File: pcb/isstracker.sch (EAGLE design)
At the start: 22 parts, among them IC1 SN74AHCT125N, IC2 L7805CV, J1 MOTOR_RIGHT, J2 MOTOR_LEFT, J4 DISPLAY, J5 CONTROL, J7 LED, J8 UART, J9 DISTANCE, U1 ARGON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

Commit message: Lots of changes
* Dropped LED's and LASER control
* Renamed DECLINATION to AZIMUTH
* Moved AZIMUTH control hookup into the globe (it needs to spin freely)

I couldn't make the LED's fit and shine without casting shadows inside
the globe. Plus, there wasn't much room, and it required more wires to
make work. No a critical problem, but the challenges outweighed the
benefits. I'm going to water color paint the globe now.

I also removed the LASER control, the manufacturer said don't duty cycle
it, the built in controls take care of it. This isn't supposed to be on
constantly anyway.
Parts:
- removed IC1: SN74AHCT125N, adafruit:74125N
- removed J2: MOTOR_LEFT, SparkFun-Connectors:CONN_11
- removed J7: LED, SparkFun-Connectors:CONN_04
- added J3: MOTOR_LEFT, SparkFun-Connectors:CONN_12
- J5: device SparkFun-Connectors:CONN_09 -> SparkFun-Connectors:CONN_08"
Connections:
- removed net CO: IC1A.O, J7.2
- removed net DO: IC1B.O, J7.3
- removed net LASER: J5.9, U1.A0
- removed net LED_CO: IC1A.I, U1.D7
- removed net LED_DO: IC1B.I, U1.D8
- net +5V: no longer IC1P.VCC, J7.4
- net AZIMUTH: now also U1.D7; no longer U1.A1
- net GND: now also J3.3; no longer IC1A.OE, IC1B.OE, IC1C.O, IC1C.OE, IC1D.O, IC1D.OE, IC1P.GND, J2.3, J7.1
- net MTR_DIR: now also J3.1; no longer J2.1
- net MTR_MS1: now also J3.10; no longer J2.10
- net MTR_SLP: now also J3.11; no longer J2.11
- net MTR_STEP: now also J3.2; no longer J2.2

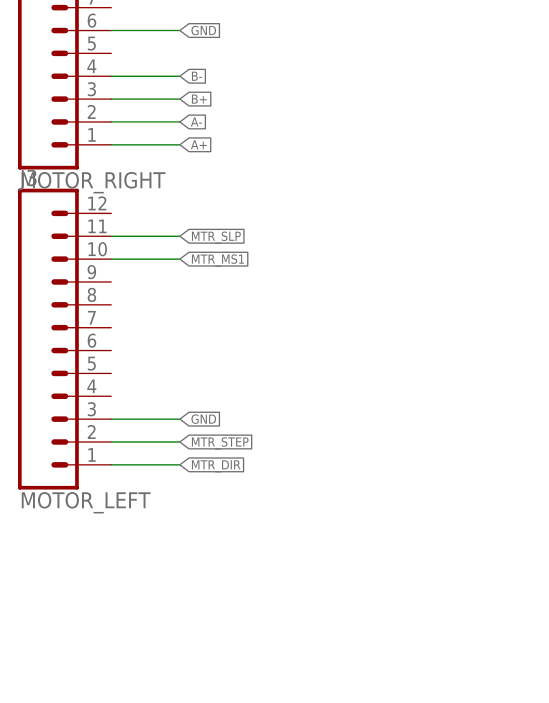
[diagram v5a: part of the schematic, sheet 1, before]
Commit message: PCB fixups
* Bumped PCB revisions
* Layout changes and some silk screen updates
* No functionality changes
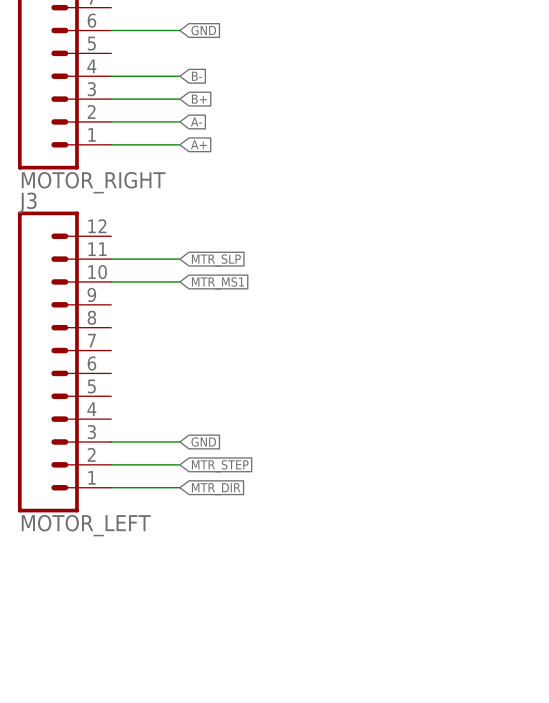
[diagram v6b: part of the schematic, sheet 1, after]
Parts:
- H1, H2, H3, H4: value STAND-OFF -> MOUNT-HOLE3.0; device SparkFun-Hardware:STAND-OFF -> holes:MOUNT-HOLE3.0
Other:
- moved on the sheet: J3
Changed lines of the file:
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@@
 <part name="LED1" library="adafruit" library_urn="urn:adsk.eagle:library:420" deviceset="LED" device="3MM" package3d_urn="urn:adsk.eagle:package:6240537/1" value="RED"/>
 <part name="R1" library="SparkFun-Resistors" library_urn="urn:adsk.eagle:library:532" deviceset="0.3OHM" device="-0805-1/8W-1%" package3d_urn="urn:adsk.eagle:package:39651/1" value="1k"/>
-<part name="H2" library="SparkFun-Hardware" library_urn="urn:adsk.eagle:library:519" deviceset="STAND-OFF" device="" package3d_urn="urn:adsk.eagle:package:38630/1"/>
-<part name="H3" library="SparkFun-Hardware" library_urn="urn:adsk.eagle:library:519" deviceset="STAND-OFF" device="" package3d_urn="urn:adsk.eagle:package:38630/1"/>
-<part name="H4" library="SparkFun-Hardware" library_urn="urn:adsk.eagle:library:519" deviceset="STAND-OFF" device="" package3d_urn="urn:adsk.eagle:package:38630/1"/>
 <part name="C2" library="SparkFun-Capacitors" library_urn="urn:adsk.eagle:library:510" deviceset="100UF-POLAR" device="-RADIAL-2.5MM-25V-20%" package3d_urn="urn:adsk.eagle:package:37415/1" value="100uF"/>
 <part name="C1" library="SparkFun-Capacitors" library_urn="urn:adsk.eagle:library:510" deviceset="100UF-POLAR" device="-RADIAL-2.5MM-25V-20%" package3d_urn="urn:adsk.eagle:package:37415/1" value="100uF"/>
-<part name="H1" library="SparkFun-Hardware" library_urn="urn:adsk.eagle:library:519" deviceset="STAND-OFF" device="" package3d_urn="urn:adsk.eagle:package:38630/1"/>
 <part name="J5" library="SparkFun-Connectors" library_urn="urn:adsk.eagle:library:513" deviceset="CONN_08" device="&quot;" package3d_urn="urn:adsk.eagle:package:38138/1" value="CONTROL"/>
 <part name="J3" library="SparkFun-Connectors" library_urn="urn:adsk.eagle:library:513" deviceset="CONN_12" device="" package3d_urn="urn:adsk.eagle:package:38169/1" value="MOTOR_LEFT"/>
+<part name="H1" library="holes" library_urn="urn:adsk.eagle:library:237" deviceset="MOUNT-HOLE" device="3.0" package3d_urn="urn:adsk.eagle:package:14277/1"/>
+<part name="H2" library="holes" library_urn="urn:adsk.eagle:library:237" deviceset="MOUNT-HOLE" device="3.0" package3d_urn="urn:adsk.eagle:package:14277/1"/>
+<part name="H3" library="holes" library_urn="urn:adsk.eagle:library:237" deviceset="MOUNT-HOLE" device="3.0" package3d_urn="urn:adsk.eagle:package:14277/1"/>
+<part name="H4" library="holes" library_urn="urn:adsk.eagle:library:237" deviceset="MOUNT-HOLE" device="3.0" package3d_urn="urn:adsk.eagle:package:14277/1"/>
 </parts>
 <sheets>
@@
 <attribute name="NAME" x="103.632" y="48.26" size="1.778" layer="95" font="vector" rot="R90"/>
 </instance>
-<instance part="J3" gate="G$1" x="10.16" y="149.86" smashed="yes">
-<attribute name="VALUE" x="10.16" y="129.794" size="1.778" layer="96" font="vector"/>
-<attribute name="NAME" x="10.16" y="165.608" size="1.778" layer="95" font="vector"/>
+<instance part="J3" gate="G$1" x="10.16" y="147.32" smashed="yes">
+<attribute name="VALUE" x="10.16" y="127.254" size="1.778" layer="96" font="vector"/>
+<attribute name="NAME" x="10.16" y="163.068" size="1.778" layer="95" font="vector"/>
 </instance>
 </instances>
@@
 </segment>
 <segment>
-<wire x1="20.32" y1="139.7" x2="27.94" y2="139.7" width="0.1524" layer="91"/>
-<label x="27.94" y="139.7" size="1.016" layer="95" xref="yes"/>
+<wire x1="20.32" y1="137.16" x2="27.94" y2="137.16" width="0.1524" layer="91"/>
+<label x="27.94" y="137.16" size="1.016" layer="95" xref="yes"/>
 <pinref part="J3" gate="G$1" pin="3"/>
 </segment>
@@
 <net name="MTR_MS1" class="0">
 <segment>
-<wire x1="20.32" y1="157.48" x2="27.94" y2="157.48" width="0.1524" layer="91"/>
-<label x="27.94" y="157.48" size="1.016" layer="95" xref="yes"/>
+<wire x1="20.32" y1="154.94" x2="27.94" y2="154.94" width="0.1524" layer="91"/>
+<label x="27.94" y="154.94" size="1.016" layer="95" xref="yes"/>
 <pinref part="J3" gate="G$1" pin="10"/>
 </segment>
@@
 <net name="MTR_STEP" class="0">
 <segment>
-<wire x1="20.32" y1="137.16" x2="27.94" y2="137.16" width="0.1524" layer="91"/>
-<label x="27.94" y="137.16" size="1.016" layer="95" xref="yes"/>
+<wire x1="20.32" y1="134.62" x2="27.94" y2="134.62" width="0.1524" layer="91"/>
+<label x="27.94" y="134.62" size="1.016" layer="95" xref="yes"/>
 <pinref part="J3" gate="G$1" pin="2"/>
 </segment>
@@
 <net name="MTR_DIR" class="0">
 <segment>
-<wire x1="20.32" y1="134.62" x2="27.94" y2="134.62" width="0.1524" layer="91"/>
-<label x="27.94" y="134.62" size="1.016" layer="95" xref="yes"/>
+<wire x1="20.32" y1="132.08" x2="27.94" y2="132.08" width="0.1524" layer="91"/>
+<label x="27.94" y="132.08" size="1.016" layer="95" xref="yes"/>
 <pinref part="J3" gate="G$1" pin="1"/>
 </segment>
@@
 <net name="MTR_SLP" class="0">
 <segment>
-<wire x1="20.32" y1="160.02" x2="27.94" y2="160.02" width="0.1524" layer="91"/>
-<label x="27.94" y="160.02" size="1.016" layer="95" xref="yes"/>
+<wire x1="20.32" y1="157.48" x2="27.94" y2="157.48" width="0.1524" layer="91"/>
+<label x="27.94" y="157.48" size="1.016" layer="95" xref="yes"/>
 <pinref part="J3" gate="G$1" pin="11"/>
 </segment>
@@
 <attribute name="VALUE" x="159.004" y="109.22" size="1.778" layer="96" font="vector" rot="R90" align="top-center"/>
 </instance>
-<instance part="H2" gate="G$1" x="10.16" y="203.2" smashed="yes"/>
-<instance part="H3" gate="G$1" x="20.32" y="203.2" smashed="yes"/>
-<instance part="H4" gate="G$1" x="25.4" y="203.2" smashed="yes"/>
 <instance part="C2" gate="G$1" x="167.64" y="121.92" smashed="yes" rot="R180">
 <attribute name="NAME" x="166.624" y="121.285" size="1.778" layer="95" font="vector" rot="R180"/>
@@
 <attribute name="VALUE" x="110.744" y="126.111" size="1.778" layer="96" font="vector" rot="R180"/>
 </instance>
-<instance part="H1" gate="G$1" x="15.24" y="203.2" smashed="yes"/>
+<instance part="H1" gate="G$1" x="27.94" y="195.58" smashed="yes">
+<attribute name="NAME" x="29.972" y="196.1642" size="1.778" layer="95"/>
+<attribute name="VALUE" x="29.972" y="193.1162" size="1.778" layer="96"/>
+</instance>
+<instance part="H2" gate="G$1" x="27.94" y="185.42" smashed="yes">
+<attribute name="NAME" x="29.972" y="186.0042" size="1.778" layer="95"/>
+<attribute name="VALUE" x="29.972" y="182.9562" size="1.778" layer="96"/>
+</instance>
+<instance part="H3" gate="G$1" x="27.94" y="172.72" smashed="yes">
+<attribute name="NAME" x="29.972" y="173.3042" size="1.778" layer="95"/>
+<attribute name="VALUE" x="29.972" y="170.2562" size="1.778" layer="96"/>
+</instance>
+<instance part="H4" gate="G$1" x="27.94" y="162.56" smashed="yes">
+<attribute name="NAME" x="29.972" y="163.1442" size="1.778" layer="95"/>
+<attribute name="VALUE" x="29.972" y="160.0962" size="1.778" layer="96"/>
+</instance>
 </instances>
 <busses>

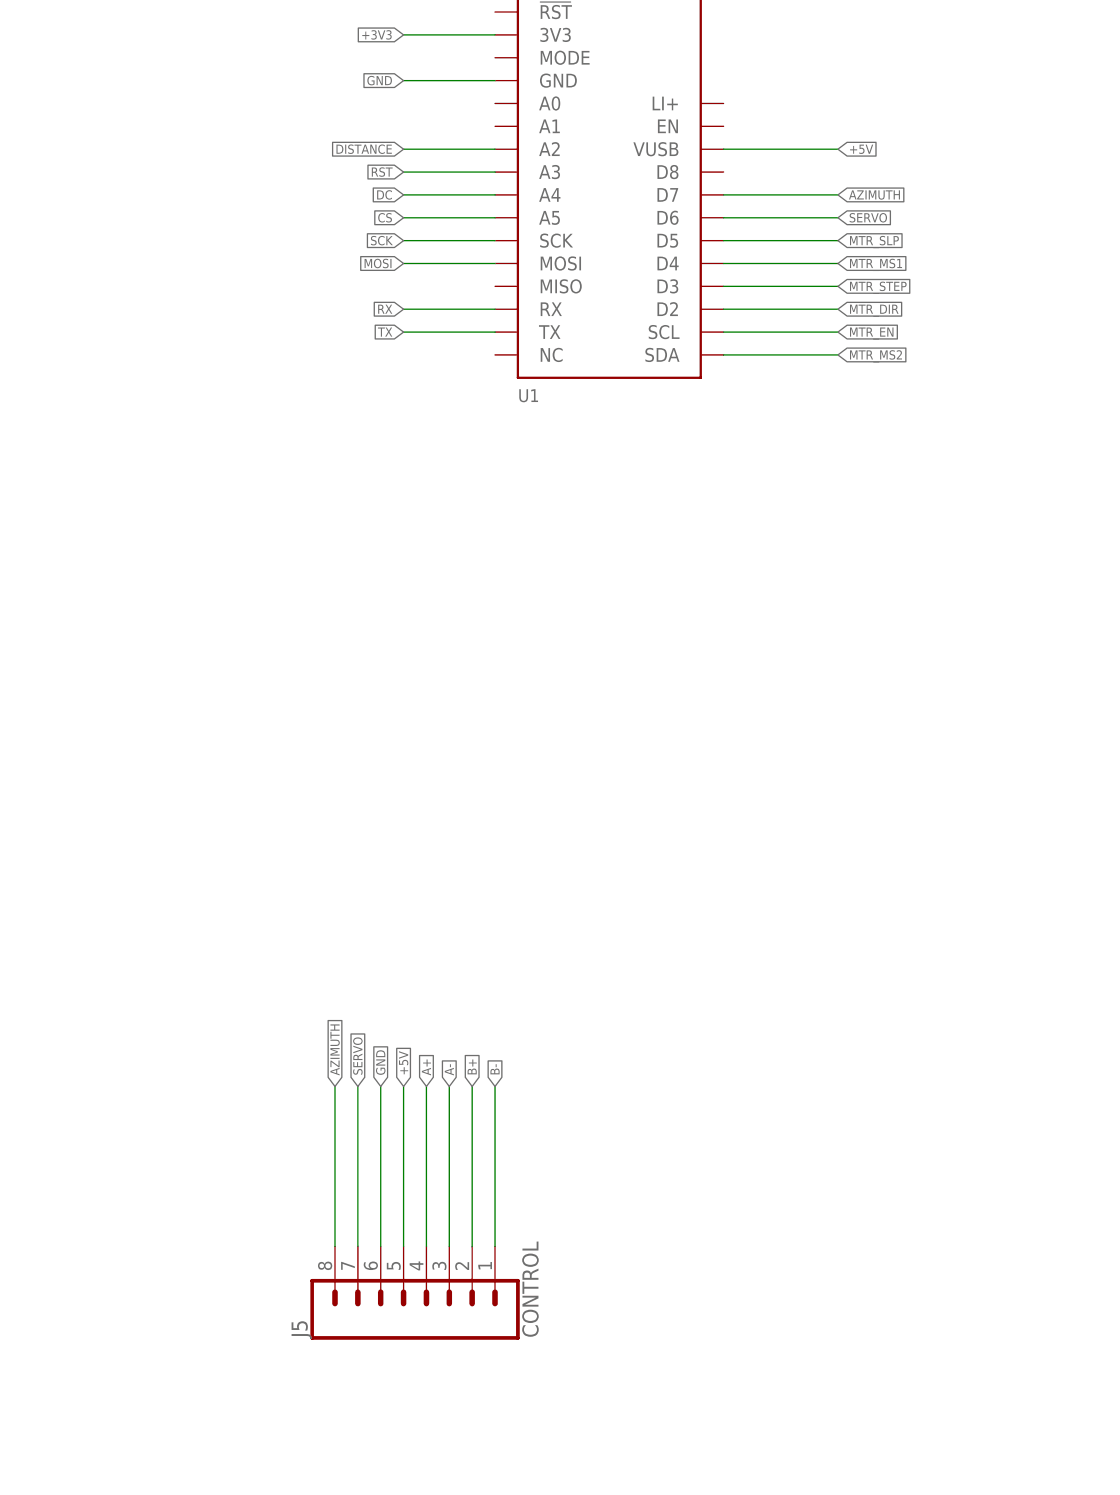
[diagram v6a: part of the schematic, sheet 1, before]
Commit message: Fixups
* Add the ability to turn the power to the globe on and off via a MOSFET
* Clean up some of the code
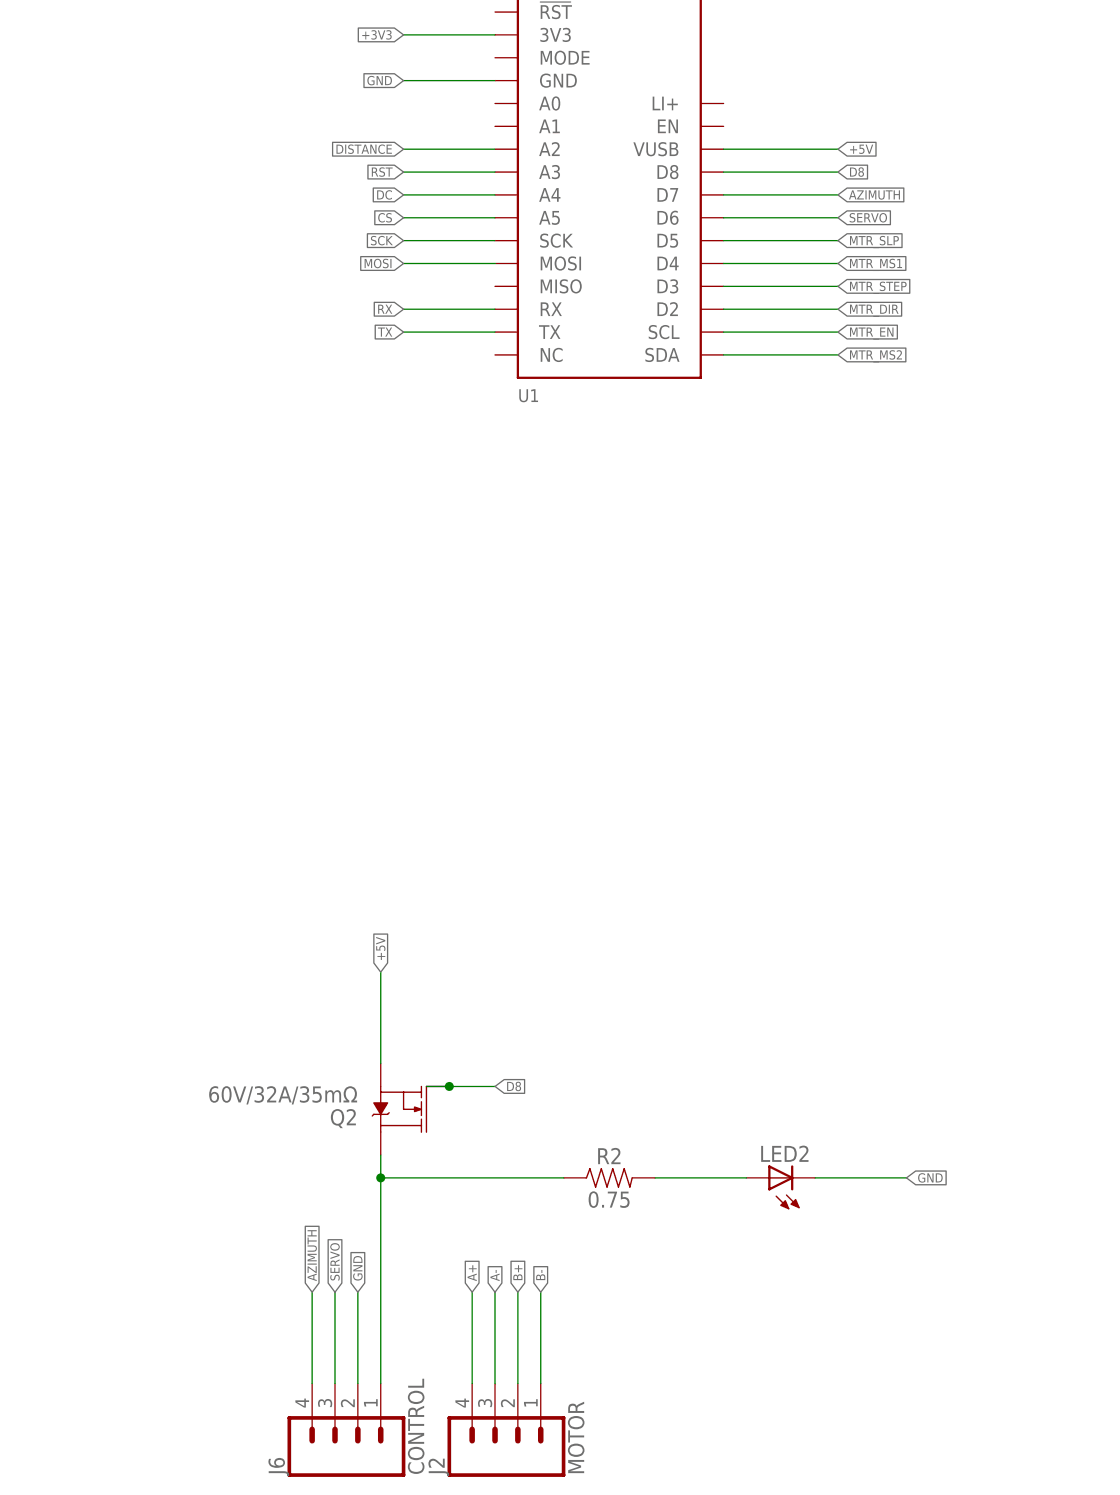
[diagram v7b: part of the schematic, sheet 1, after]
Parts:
- removed J5: CONTROL, SparkFun-Connectors:CONN_08"
- removed LED3: BLUE, adafruit:LED3MM
- added J2: MOTOR, SparkFun-Connectors:CONN_04
- added J6: CONTROL, SparkFun-Connectors:CONN_04
- added LED2: (no value), adafruit:LED3MM
- added Q2: 60V/32A/35mΩ, SparkFun-DiscreteSemi:MOSFET-NCH-FQP30N06L
- R2: value 1k -> 0.75; device SparkFun-Resistors:0.3OHM-0805-1/8W-1% -> SparkFun-Resistors:0.75OHM-0805-1/4W-1%
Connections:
- new net D8: Q2.G, U1.D8
- new net N$3: J6.1, Q2.D, R2.1
- net +5V: now also Q2.S; no longer J5.5, LED3.A
- net A+: now also J2.4; no longer J5.4
- net A-: now also J2.3; no longer J5.3
- net AZIMUTH: now also J6.4; no longer J5.8
- net B+: now also J2.2; no longer J5.2
- net B-: now also J2.1; no longer J5.1
- net GND: now also J6.2, LED2.C; no longer J5.6, R2.1
- net N$4: now also LED2.A; no longer LED3.C
- net SERVO: now also J6.3; no longer J5.7
